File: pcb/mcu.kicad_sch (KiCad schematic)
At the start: 24 parts, among them J1 Debug, U7 ESP32-C6-WROOM-1-N8, X1 Q13FC1350000400

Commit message: sch: remove aht20 temp humidity sensor
Fixes #49
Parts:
- removed R15, R16: 10kΩ, PCM_JLCPCB:R_0603, symbol PCM_JLCPCB-Resistors:0603,10kΩ
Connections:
- net SCL: no longer names the net of U7.12 (IO11)
- net SDA: no longer names the net of U7.11 (IO10)
- no-connect marks 3 -> 5
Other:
- note removed: "I2C Pullup"
- moved on the sheet: D12, J1, R20, R21, R22

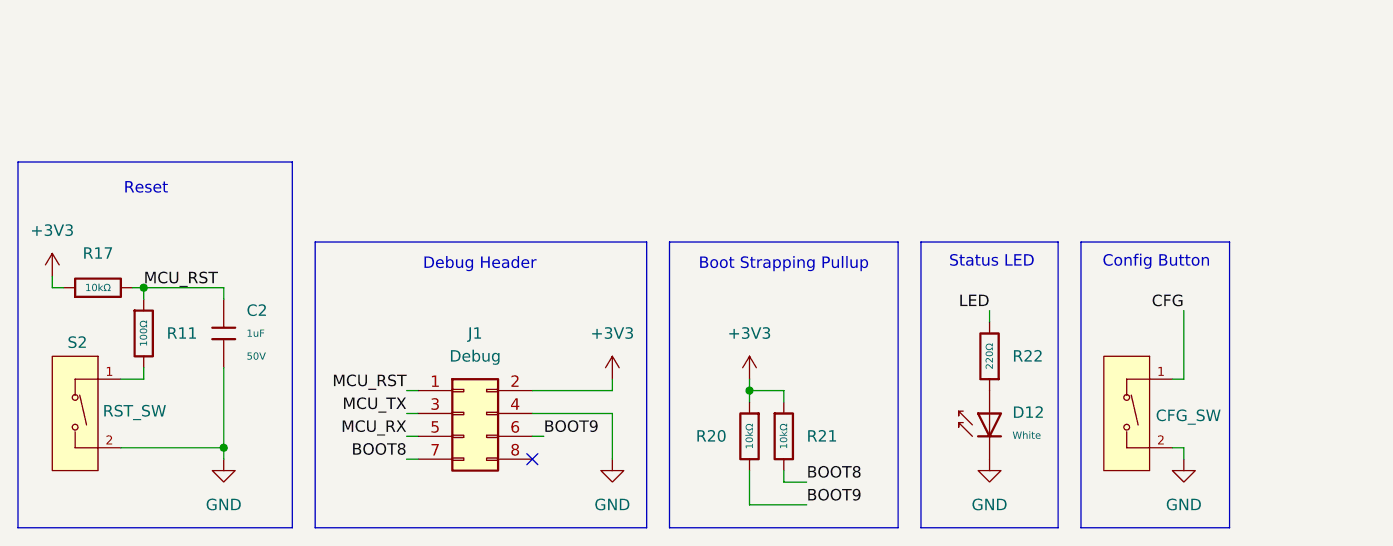
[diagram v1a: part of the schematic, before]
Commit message: sch: remove reset switch
It's reasonable to power cycle the device to reset it, or use the programming header/USB C when flashing. This improves moisture resilience, reduces cost and simplifies the design.
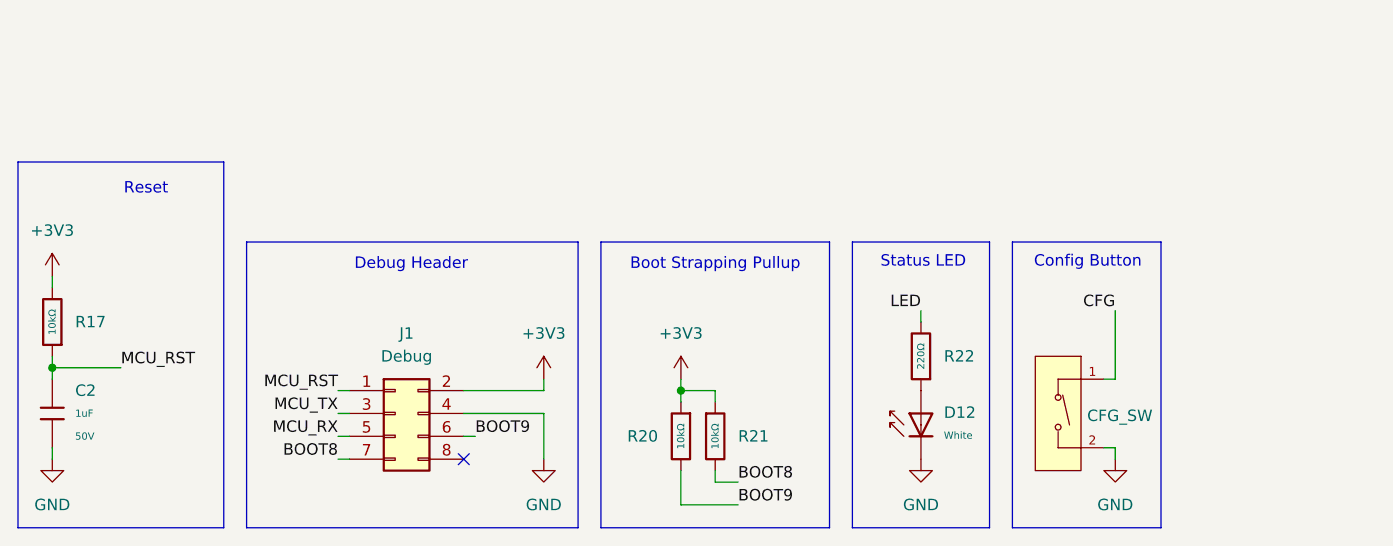
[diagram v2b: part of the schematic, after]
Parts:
- removed R11: 100Ω, PCM_JLCPCB:R_0603, symbol PCM_JLCPCB-Resistors:0603,100Ω
- removed S2: Tactile Button, 160gf, PCM_JLCPCB:SW_TS-1088-AR02016, symbol EasyEDA:Tactile_Button,_160gf,_12V,_50mA,_4.0mm
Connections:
- net +3V3: now also R17.2; no longer R17.1
- net MCU_RST: now also R17.1; no longer R17.2
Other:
- moved on the sheet: C2, D12, J1, R17, R20, R21, R22

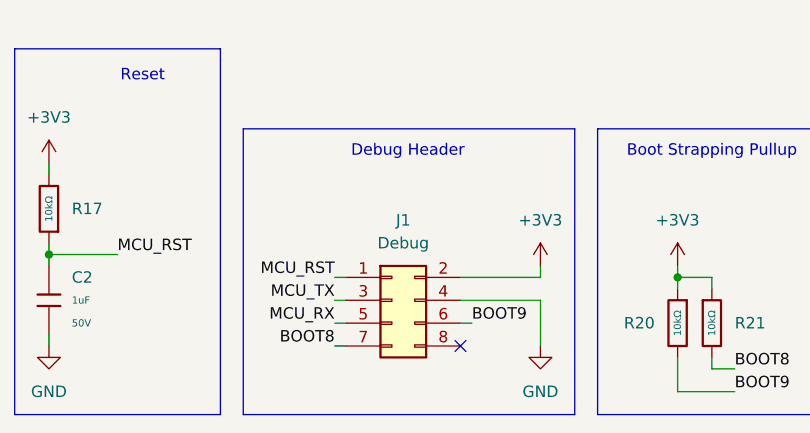
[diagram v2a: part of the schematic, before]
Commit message: sch: revert debug/flash header to espprog format
Had previously added IO8 to this header, but have confirmed it's not needed for flashing via UART. The header is now ESPPROG compatible, and I've confirmed flashing works with an ESPPROG flasher device on the V1 board revision which uses the same pinout. Fixes #50
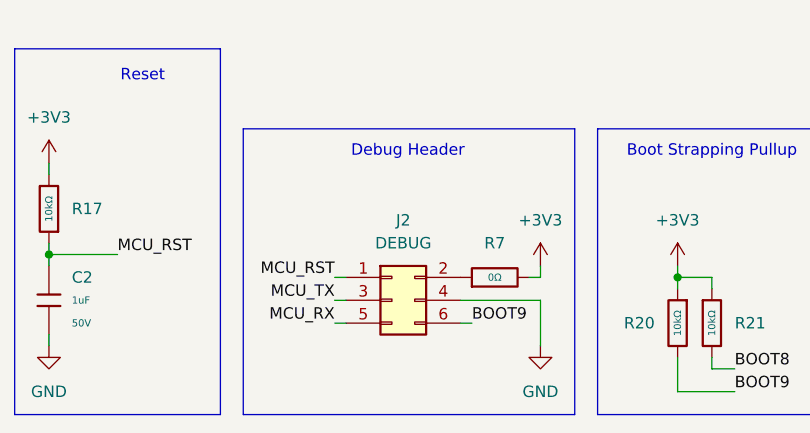
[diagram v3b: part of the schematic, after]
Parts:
- removed J1: Debug, Connector_PinHeader_2.54mm:PinHeader_2x04_P2.54mm_Vertical, symbol Connector_Generic:Conn_02x04_Odd_Even
- added J2: DEBUG, Connector_PinHeader_2.54mm:PinHeader_2x03_P2.54mm_Vertical, symbol Connector_Generic:Conn_02x03_Odd_Even
- added R7: 0Ω, PCM_JLCPCB:R_0603, symbol PCM_JLCPCB-Resistors:0603,0Ω
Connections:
- net +3V3: now also R7.2
- net BOOT9: now also J2.6 (Pin_6)
- net GND: now also J2.4 (Pin_4)
- net MCU_RST: now also J2.1 (Pin_1)
- net MCU_RX: now also J2.5 (Pin_5)
- net MCU_TX: now also J2.3 (Pin_3)
- new net: J2.2 (Pin_2), R7.1
- no-connect marks 5 -> 4

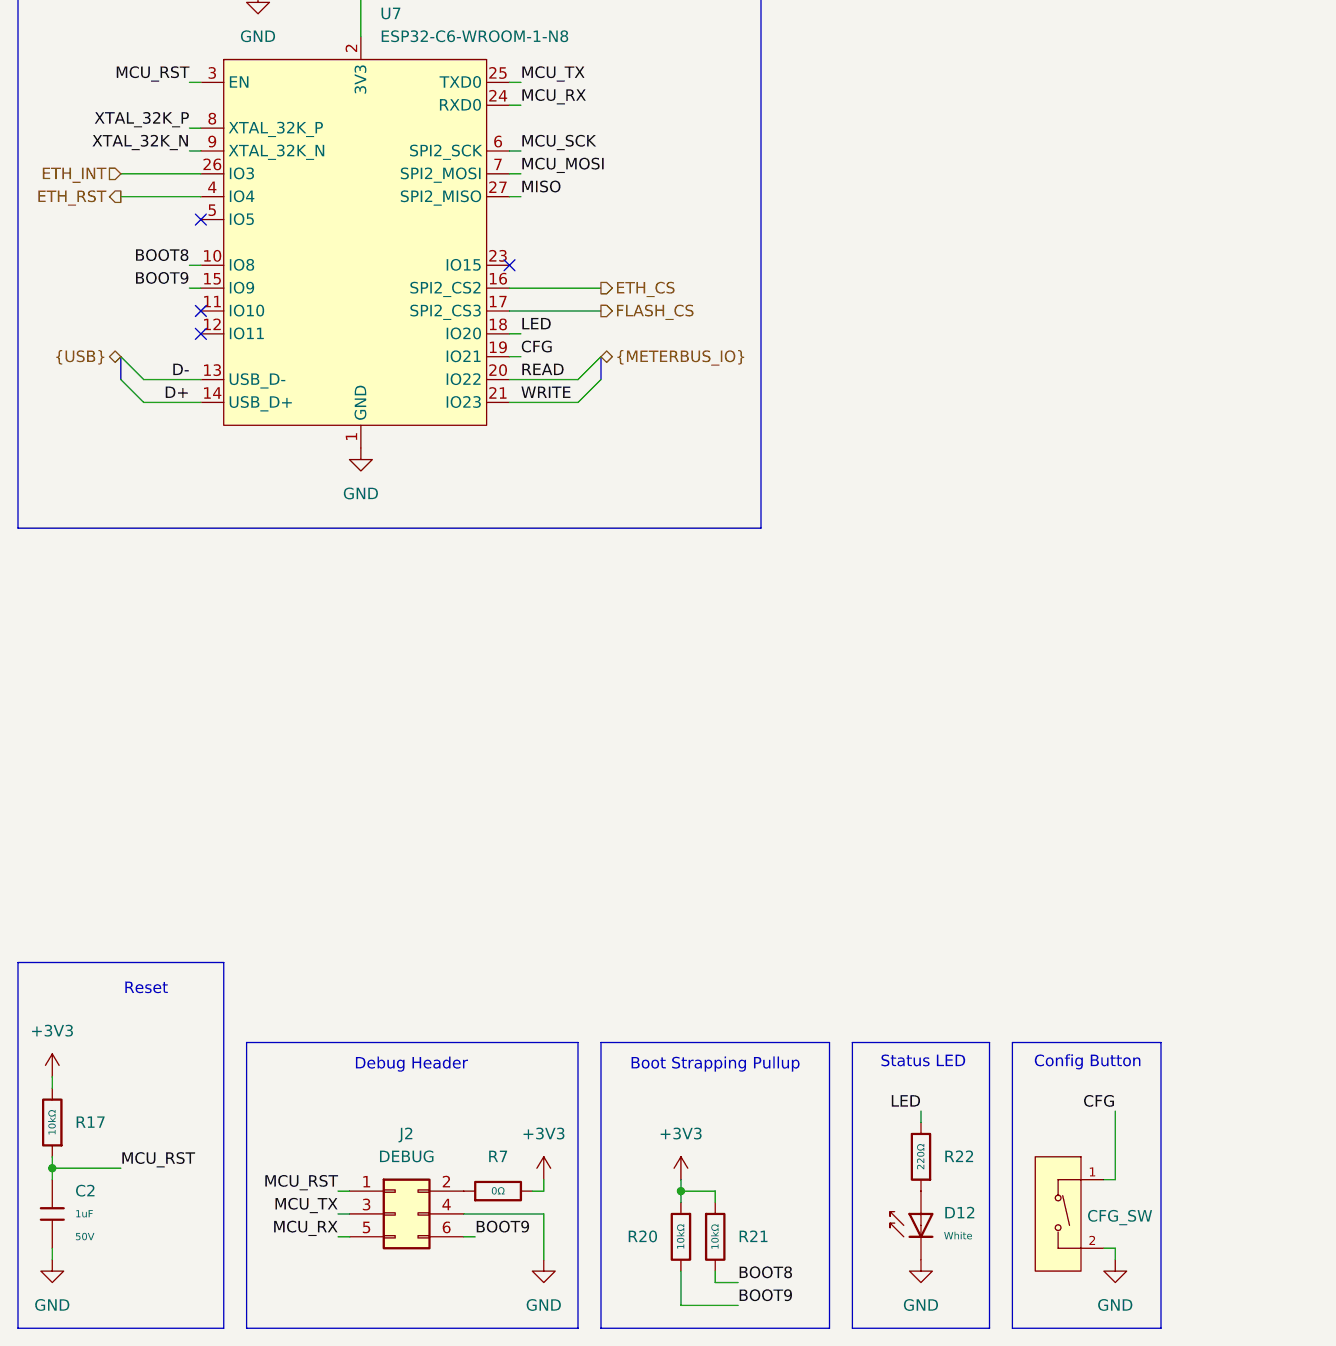
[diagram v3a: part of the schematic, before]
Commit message: sch: highlight esp strapping pins and avoid using them
Moves the ETH_INT and ETH_RST pins to avoid the strapping pins on the
ESP, and also adds a pullup on IO15 to avoid edge case where JTAG source
efuse is set and the pin is left floating which could disrupt USB JTAG.

Fixes #26
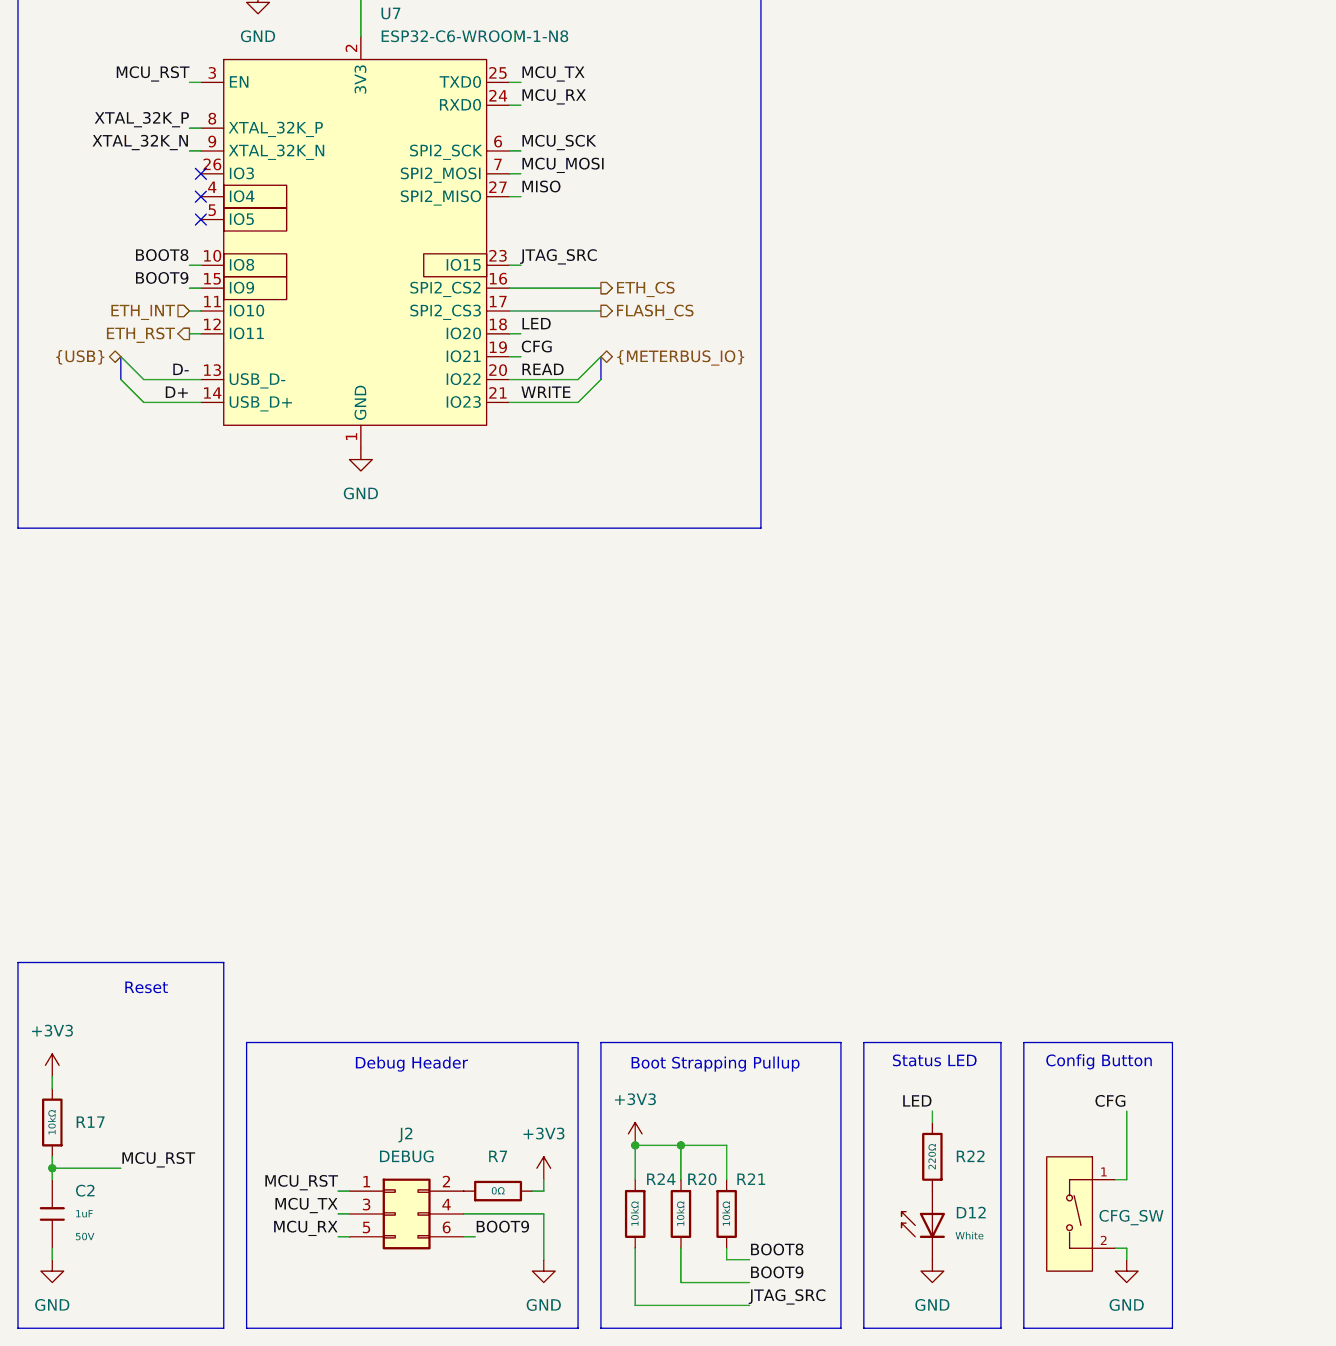
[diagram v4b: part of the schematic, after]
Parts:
- added R24: 10kΩ, PCM_JLCPCB:R_0603, symbol PCM_JLCPCB-Resistors:0603,10kΩ
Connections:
- net +3V3: now also R24.1
- net ETH_INT: now also U7.11 (IO10); no longer U7.26 (IO3)
- net ETH_RST: now also U7.12 (IO11); no longer U7.4 (IO4)
- net JTAG_SRC: now reaches U7.23 (IO15)
- net JTAG_SRC: now also R24.2
- no-connect marks 4 -> 3
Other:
- moved on the sheet: D12, R20, R21, R22

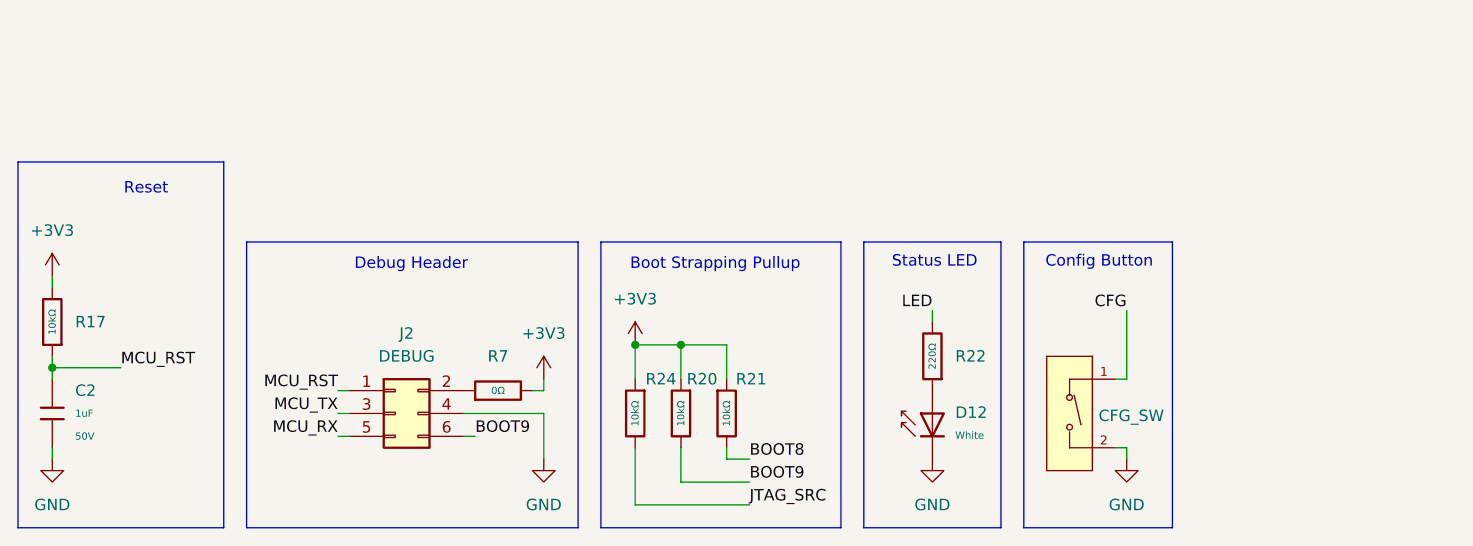
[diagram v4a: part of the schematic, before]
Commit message: sch: reset esp32 using dc-dc pgood line
This avoids the needs for a voltage supervisor, and provides some protection against brownouts and glitches
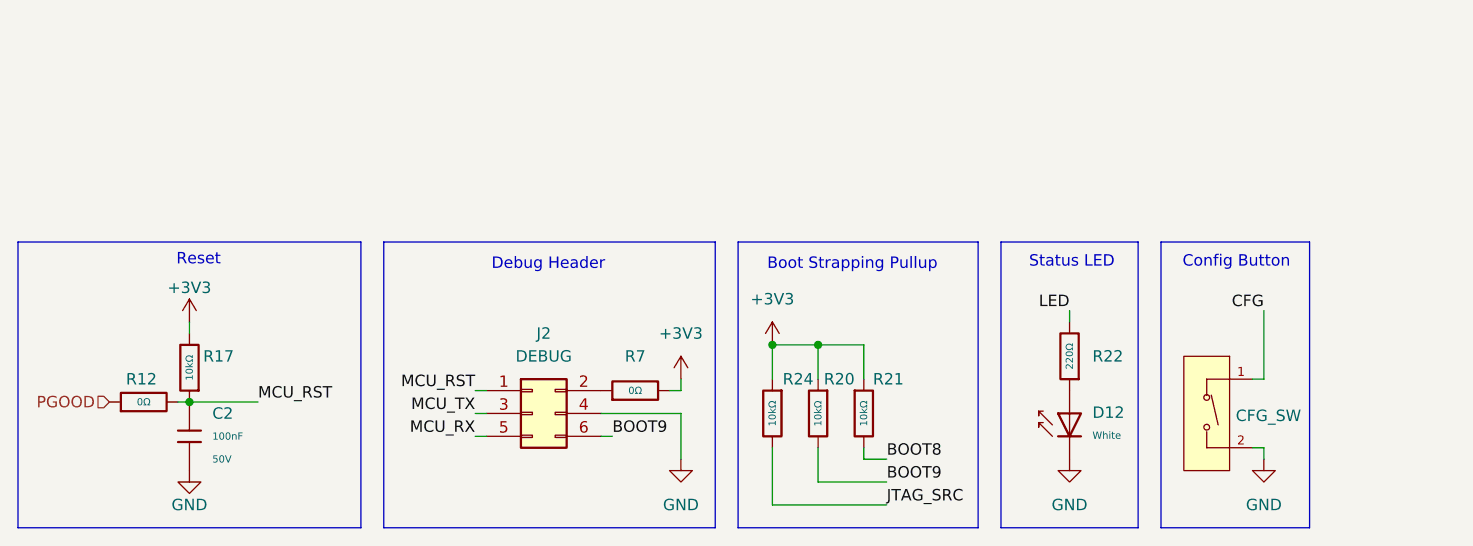
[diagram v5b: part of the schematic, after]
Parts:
- removed C2: 1uF, PCM_JLCPCB:C_0603, symbol PCM_JLCPCB-Capacitors:0603,1uF
- added C2: 100nF, PCM_JLCPCB:C_0603, symbol PCM_JLCPCB-Capacitors:0603,100nF
- added R12: 0Ω, PCM_JLCPCB:R_0603, symbol PCM_JLCPCB-Resistors:0603,0Ω
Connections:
- net GND: now also C2.2
- net MCU_RST: now also C2.1, R12.2
- new net PGOOD: R12.1
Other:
- moved on the sheet: D12, J2, R17, R20, R21, R22, R24, R7

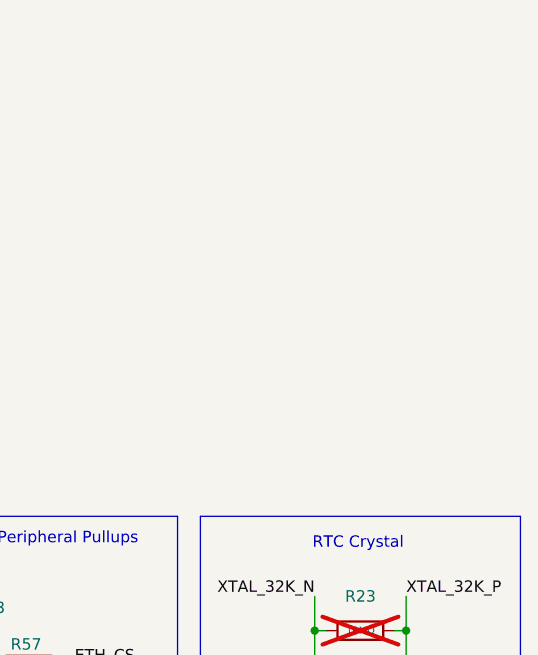
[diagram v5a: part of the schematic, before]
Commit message: sch: adjust test points
Removes some test points, and adds useful ones to data lines. Fixes #19
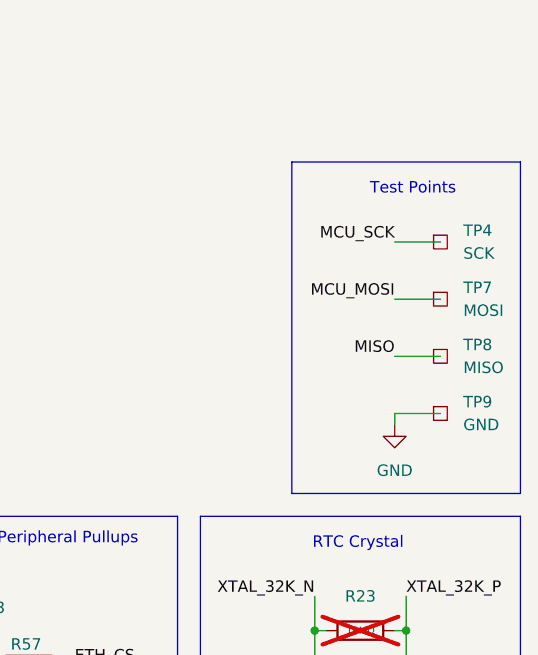
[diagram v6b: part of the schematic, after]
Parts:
- added TP4: SCK, TestPoint:TestPoint_Pad_D1.0mm, symbol Connector:TestPoint_Square
- added TP7: MOSI, TestPoint:TestPoint_Pad_D1.0mm, symbol Connector:TestPoint_Square
- added TP8: MISO, TestPoint:TestPoint_Pad_D1.0mm, symbol Connector:TestPoint_Square
- added TP9: GND, TestPoint:TestPoint_Plated_Hole_D2.0mm, symbol Connector:TestPoint_Square
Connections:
- net GND: now also TP9.1
- net MCU_MOSI: now also TP7.1
- net MCU_SCK: now also TP4.1
- net MISO: now also TP8.1
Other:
- note added: "Test Points"

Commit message: sch: add schematic titles and do some cleanup
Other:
- company: (none) -> CIA Assured
- title: (none) -> Processor
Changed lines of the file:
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@@
 	(generator_version "10.0")
 	(paper "A4")
+	(title_block
+		(title "Processor")
+		(company "CIA Assured")
+	)
 	(rectangle
 		(start 15.24 162.56)
